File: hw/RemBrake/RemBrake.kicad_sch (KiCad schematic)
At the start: 3 parts, among them J1 Screw_Terminal_01x04, J2 Screw_Terminal_01x02

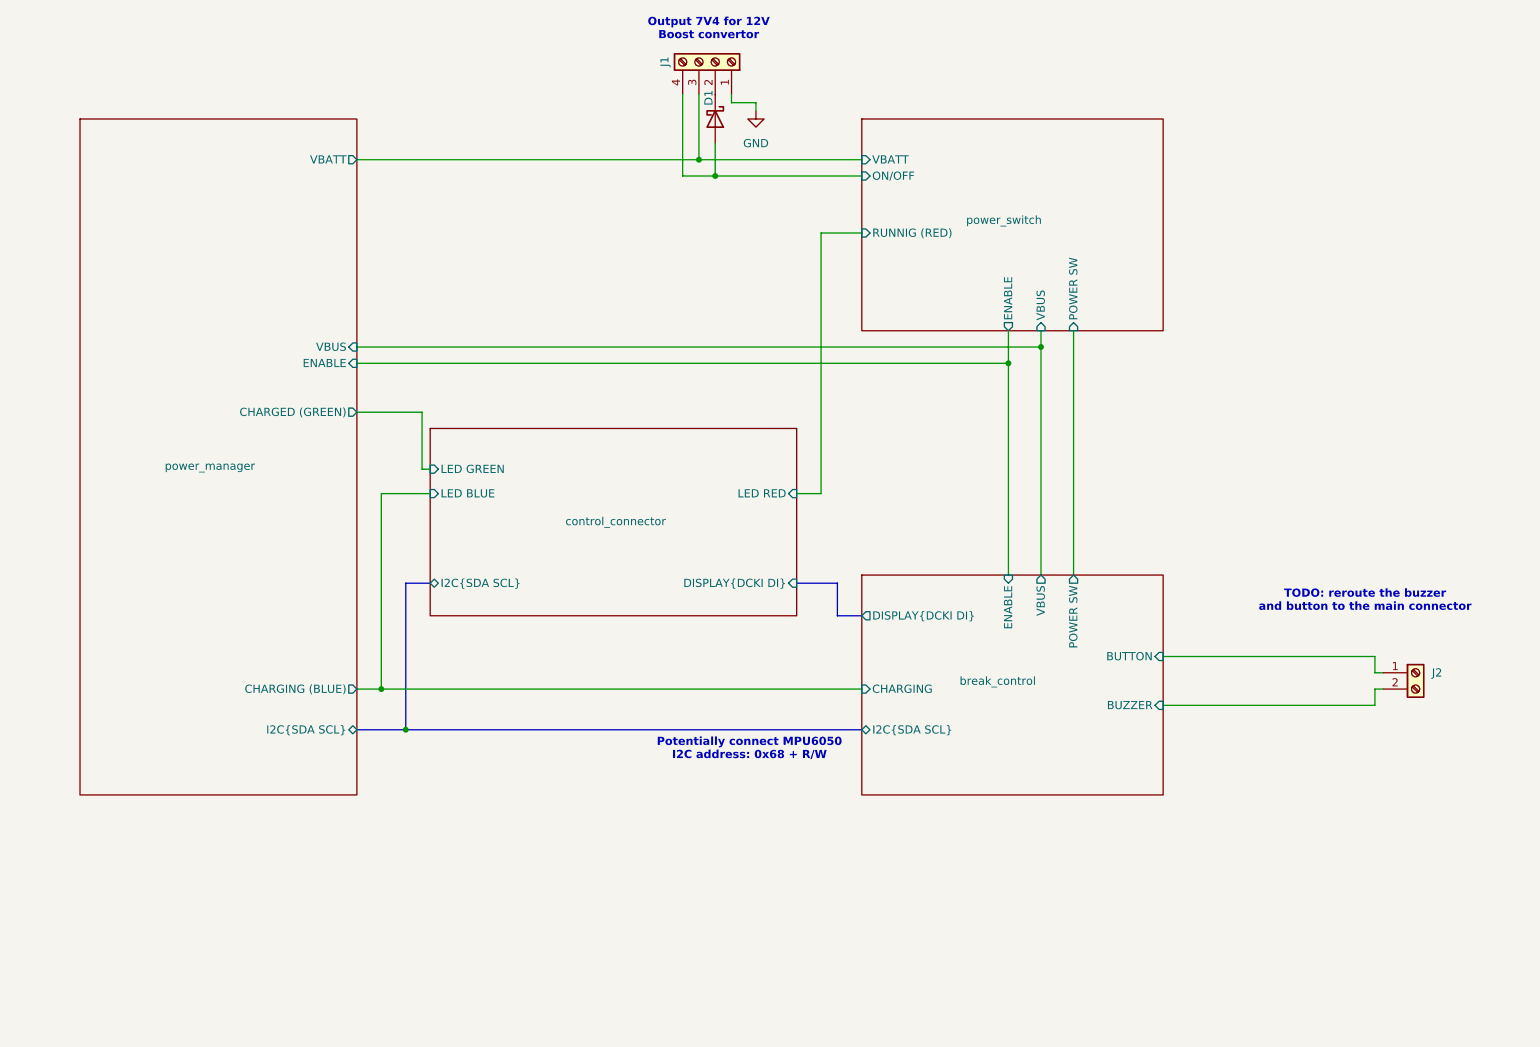
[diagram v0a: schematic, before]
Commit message: project renamed, schematics changed based on breakout boards notes and created new layout with better connectors
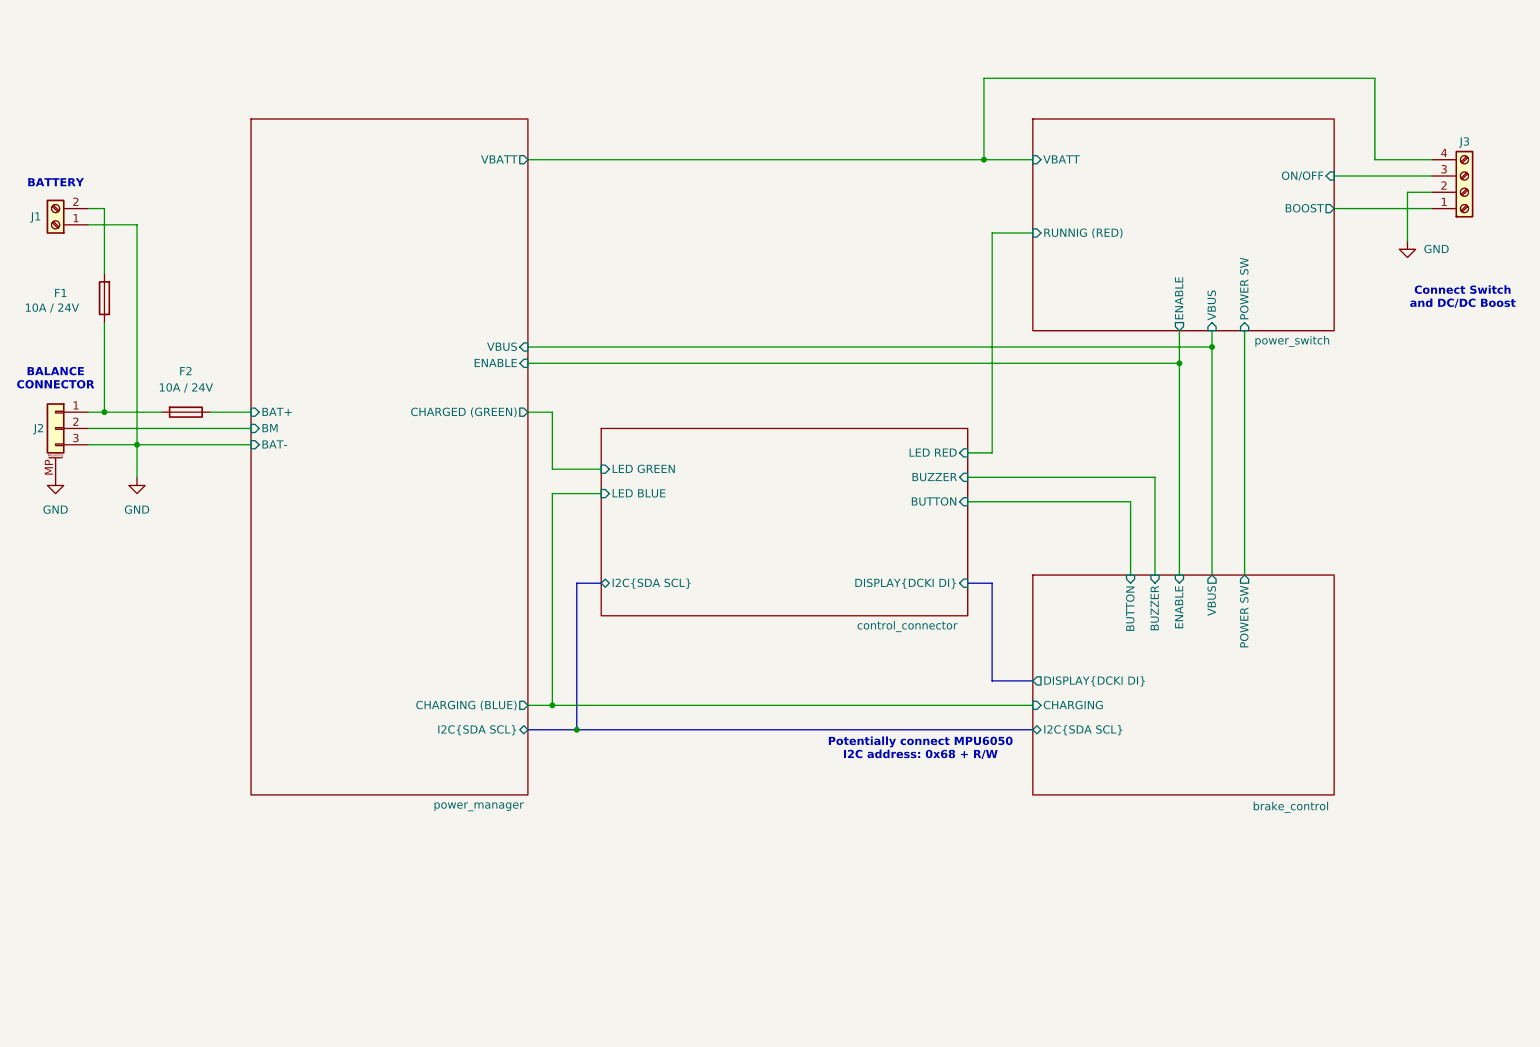
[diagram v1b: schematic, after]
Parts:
- removed D1: D_Schottky, symbol Device:D_Schottky
- removed J2: Screw_Terminal_01x02, symbol Connector:Screw_Terminal_01x02
- added F1, F2: 10A / 24V, Fuse:Fuse_1206_3216Metric_Pad1.42x1.75mm_HandSolder, symbol Device:Fuse
- added J1: Screw_Terminal_01x02, TerminalBlock_Phoenix:TerminalBlock_Phoenix_MKDS-1,5-2_1x02_P5.00mm_Horizontal, symbol Connector:Screw_Terminal_01x02
- added J2: Conn_01x03_MountingPin, Connector_JST:JST_XH_S3B-XH-SM4-TB_1x03-1MP_P2.50mm_Horizontal, symbol Connector_Generic_MountingPin:Conn_01x03_MountingPin
- renumbered J1 to J3
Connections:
- net GND: now also J3.2 (Pin_2), J1.1 (Pin_1), J2.3 (Pin_3), J2.MP (MountPin); no longer J3.1 (Pin_1)
- net power_manager/VBATT: now also J3.4 (Pin_4); no longer J3.3 (Pin_3)
- net power_switch/ON/OFF: now also J3.3 (Pin_3); no longer J3.4 (Pin_4)
- new net: F1.1, F2.2, J2.1 (Pin_1)
- new net: F1.2, J1.2 (Pin_2)
- new net power_manager/BAT+: F2.1
- new net power_manager/BM: J2.2 (Pin_2)
- new net power_switch/BOOST: J3.1 (Pin_1)
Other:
- sheet break_control renamed brake_control
- sheet brake_control: file break_control.kicad_sch -> brake_control.kicad_sch
- sheet control_connector ports: added BUTTON, BUZZER; removed none
- sheet power_manager ports: added BAT+, BAT-, BM; removed none
- sheet power_switch ports: added BOOST; removed none
- note added: "BALANCE CONNECTOR"
- note added: "BATTERY"
- note added: "Connect Switch and DC/DC Boost"
- note removed: "Output 7V4 for 12V Boost convertor"
- note removed: "TODO: reroute the buzzer and button to the main connector"
- title: Remote Break Main Board -> Remote Brake Main Board
- moved on the sheet: J3

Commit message: updated routing yet need to do some small adjustment of the polygon priorities
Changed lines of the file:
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@@
+	)
+	(symbol
+		(lib_id "Graphic:Logo_Open_Hardware_Small")
+		(at 152.4 181.61 0)
+		(unit 1)
+		(exclude_from_sim yes)
+		(in_bom no)
+		(on_board yes)
+		(dnp no)
+		(fields_autoplaced yes)
+		(property "Reference" "#SYM1"
+			(at 152.4 174.625 0)
+			(hide yes)
+			(effects
+				(font
+					(size 1.27 1.27)
+				)
+			)
+		)
+		(property "Value" "Logo_Open_Hardware_Small"
+			(at 152.4 187.325 0)
+			(hide yes)
+			(effects
+				(font
+					(size 1.27 1.27)
+				)
+			)
+		)
+		(property "Footprint" ""
+			(at 152.4 181.61 0)
+			(hide yes)
+			(effects
+				(font
+					(size 1.27 1.27)
+				)
+			)
+		)
+		(property "Datasheet" "~"
+			(at 152.4 181.61 0)
+			(hide yes)
+			(effects
+				(font
+					(size 1.27 1.27)
+				)
+			)
+		)
+		(property "Description" "Open Hardware logo, small"
+			(at 152.4 181.61 0)
+			(hide yes)
+			(effects
+				(font
+					(size 1.27 1.27)
+				)
+			)
+		)
+		(instances
+			(project ""
+				(path "/e6d4ae5b-c9d7-4cbe-b288-c929fdf55a75"
+					(reference "#SYM1")
+					(unit 1)
+				)
+			)
+		)
 	)
 	(symbol

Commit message: updated date and revision in the schematics
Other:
- company: (none) -> Pacner Bros Tech
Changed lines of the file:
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@@
 	(title_block
 		(title "Remote Brake Main Board")
-		(date "2024-12-15")
-		(rev "1.0")
+		(date "2025-02-23")
+		(rev "2.0")
+		(company "Pacner Bros Tech")
 	)
 	(bus_alias "I2C"
@@
 					(unit 1)
 				)
-			)
-		)
-	)
-	(symbol
-		(lib_id "Graphic:Logo_Open_Hardware_Small")
-		(at 152.4 181.61 0)
-		(unit 1)
-		(exclude_from_sim yes)
-		(in_bom no)
-		(on_board yes)
-		(dnp no)
-		(fields_autoplaced yes)
-		(property "Reference" "#SYM1"
-			(at 152.4 174.625 0)
-			(hide yes)
-			(effects
-				(font
-					(size 1.27 1.27)
-				)
-			)
-		)
-		(property "Value" "Logo_Open_Hardware_Small"
-			(at 152.4 187.325 0)
-			(hide yes)
-			(effects
-				(font
-					(size 1.27 1.27)
-				)
-			)
-		)
-		(property "Footprint" ""
-			(at 152.4 181.61 0)
-			(hide yes)
-			(effects
-				(font
-					(size 1.27 1.27)
-				)
-			)
-		)
-		(property "Datasheet" "~"
-			(at 152.4 181.61 0)
-			(hide yes)
-			(effects
-				(font
-					(size 1.27 1.27)
-				)
-			)
-		)
-		(property "Description" "Open Hardware logo, small"
-			(at 152.4 181.61 0)
-			(hide yes)
-			(effects
-				(font
-					(size 1.27 1.27)
-				)
-			)
-		)
-		(instances
-			(project ""
-				(path "/e6d4ae5b-c9d7-4cbe-b288-c929fdf55a75"
-					(reference "#SYM1")
-					(unit 1)
-				)

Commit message: replaced optocoupler with transistor and loaded components in the pcb sheet
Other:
- sheet brake_control ports: added RUNNIG (RED); removed none
- sheet power_switch ports: added none; removed RUNNIG (RED)
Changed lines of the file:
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@@
 (kicad_sch
-	(version 20250222)
+	(version 20250227)
 	(generator "eeschema")
 	(generator_version "9.99")
@@
 	(wire
 		(pts
+			(xy 184.15 127) (xy 187.96 127)
+		)
+		(stroke
+			(width 0)
+			(type default)
+		)
+	)
+	(wire
+		(pts
 			(xy 246.38 54.61) (xy 250.19 54.61)
 		)
@@
 	(wire
 		(pts
+			(xy 177.8 106.68) (xy 184.15 106.68)
+		)
+		(stroke
+			(width 0)
+			(type default)
+		)
+	)
+	(wire
+		(pts
 			(xy 40.64 88.9) (xy 43.18 88.9)
 		)
@@
 	(wire
 		(pts
-			(xy 177.8 95.25) (xy 181.61 95.25)
-		)
-		(stroke
-			(width 0)
-			(type default)
-		)
-	)
-	(wire
-		(pts
 			(xy 220.98 76.2) (xy 220.98 114.3)
 		)
@@
 	(wire
 		(pts
-			(xy 181.61 60.96) (xy 187.96 60.96)
-		)
-		(stroke
-			(width 0)
-			(type default)
-		)
-	)
-	(wire
-		(pts
-			(xy 181.61 95.25) (xy 181.61 60.96)
-		)
-		(stroke
-			(width 0)
-			(type default)
-		)
-	)
-	(wire
-		(pts
 			(xy 180.34 49.53) (xy 187.96 49.53)
 		)
@@
 		(pts
 			(xy 109.22 134.62) (xy 113.03 134.62)
+		)
+		(stroke
+			(width 0)
+			(type default)
+		)
+	)
+	(wire
+		(pts
+			(xy 184.15 106.68) (xy 184.15 127)
 		)
 		(stroke
@@
 			)
 		)
-		(pin "RUNNIG (RED)" input
-			(at 187.96 60.96 180)
-			(effects
-				(font
-					(size 1.27 1.27)
-				)
-				(justify left)
-			)
-		)
 		(pin "ON{slash}OFF" input
 			(at 234.95 52.07 0)
@@
 			)
 		)
+		(pin "RUNNIG (RED)" input
+			(at 187.96 127 180)
+			(effects
+				(font
+					(size 1.27 1.27)
+				)
+				(justify left)
+			)
+		)
 		(instances
 			(project "RemBrake"
@@
 		)
 		(pin "LED RED" input
-			(at 177.8 95.25 0)
-			(effects
-				(font
+			(at 177.8 106.68 0)
+			(effects
+				(font
